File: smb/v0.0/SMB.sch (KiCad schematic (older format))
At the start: 24 parts, among them IC101 ATMEGA1284-A, J102 RTS_RESET, J103 ICSP, J104 SERIAL_REV, P101 I2C_CONN, P102 CONN_6, P103 CONN_5X2, P104 CONN_5X2, SW101 SKQGAKE010, X101 16MHz

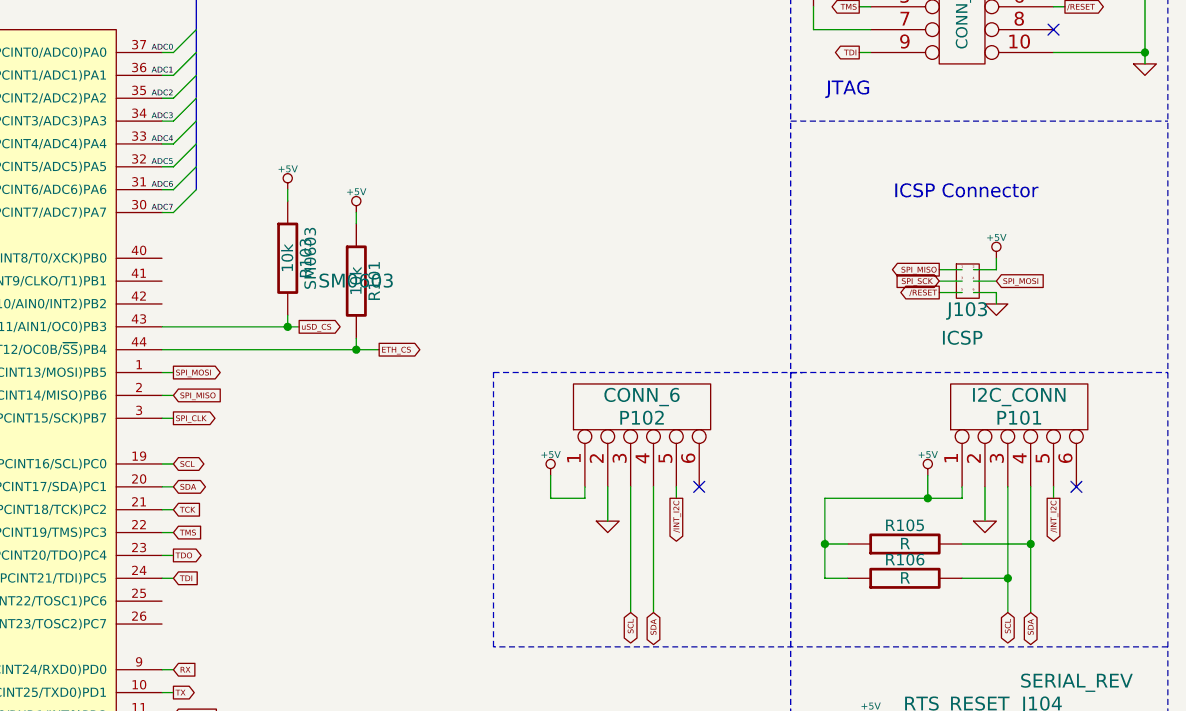
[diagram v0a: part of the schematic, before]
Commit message: Add /spare signal to the pin number 6 of the I2C connector Add silkscreen
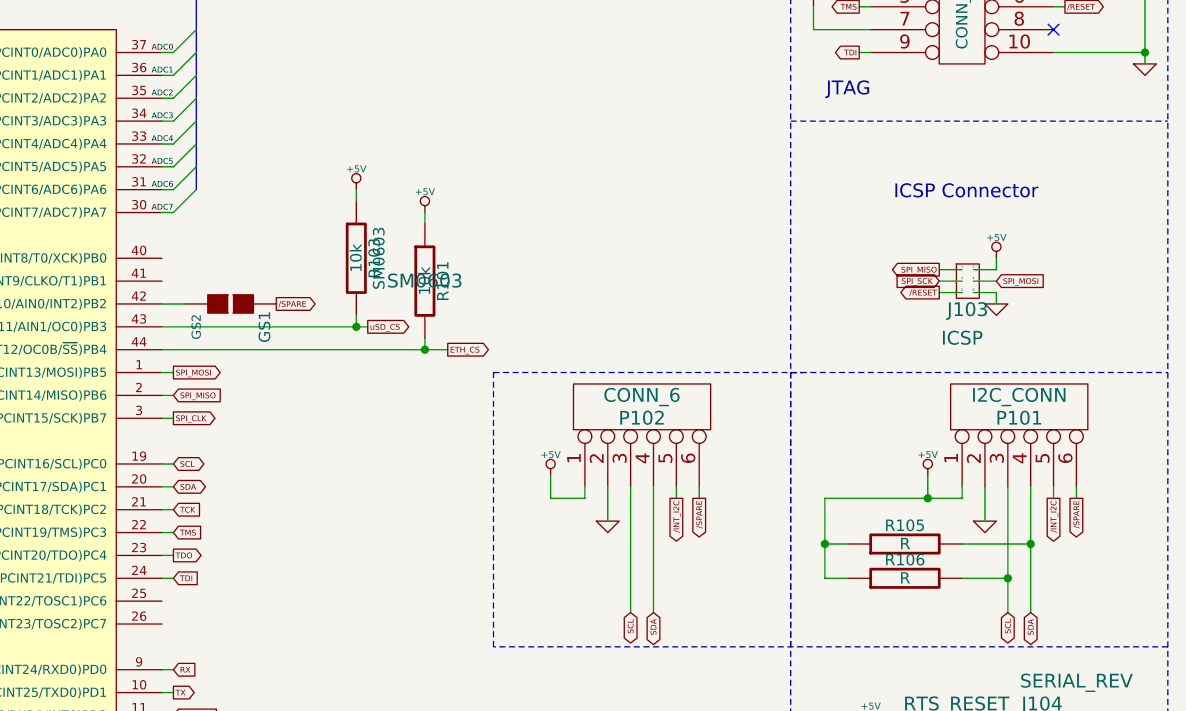
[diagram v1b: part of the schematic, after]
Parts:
- added GS1: GS2, symbol GS2
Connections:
- net at IC101.42 ((PCINT10/AIN0/INT2)PB2): now also GS1.2 (G2)
- net /SPARE: now reaches P101.6
- net /SPARE: now also P102.6, GS1.1 (G1)
- no-connect marks 3 -> 1
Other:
- moved on the sheet: R101, R103
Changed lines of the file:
@@
-EESchema Schematic File Version 2  date 09/08/2012 22:13:26
+EESchema Schematic File Version 2  date mer. 29 août 2012 13:03:19 CEST
 LIBS:power
 LIBS:device
@@
 EELAYER 25  0
 EELAYER END
-$Descr A4 11700 8267
+$Descr A4 11693 8268
 encoding utf-8
 Sheet 1 4
 Title ""
-Date "9 aug 2012"
+Date "29 aug 2012"
 Rev ""
 Comp ""
@@
 	6850 1750 6900 1750
 Wire Wire Line
-	6550 3400 7500 3400
+	6550 3400 7800 3400
 Wire Notes Line
 	10950 1400 10950 6150
@@
 	10150 4000 10150 4150
 Wire Wire Line
-	7100 2700 7100 2750
+	7400 2700 7400 2750
 Wire Notes Line
 	9300 2400 10950 2400
@@
 Wire Notes Line
 	9300 6150 10950 6150
-Connection ~ 7400 3400
-Wire Wire Line
-	7400 3350 7400 3400
+Connection ~ 7700 3400
+Wire Wire Line
+	7700 3350 7700 3400
 Wire Wire Line
 	6600 5100 6550 5100
@@
 	6600 4900 6550 4900
 Wire Wire Line
-	7400 2800 7400 2850
+	7700 2800 7700 2850
 Wire Wire Line
 	6600 4000 6550 4000
@@
 	9950 3050 10050 3050
 Wire Wire Line
-	7100 3250 7100 3300
-Connection ~ 7100 3300
+	7400 3250 7400 3300
+Connection ~ 7400 3300
 Wire Wire Line
 	9900 4050 9900 3950
@@
 	10450 1900 10500 1900
 Wire Wire Line
-	6550 3300 7150 3300
+	6550 3300 7450 3300
 Wire Wire Line
 	7700 1750 7750 1750
@@
 	1    0    0    -1
 $EndComp
-NoConn ~ 8900 4000
 $Comp
 L CONN_6 P102
@@
 	0    -1   -1   0
 $EndComp
-NoConn ~ 10550 4000
 $Comp
 L +5V #PWR08
@@
 L +5V #PWR010
 U 1 1 4FF09080
-P 7100 2700
-F 0 "#PWR010" H 7100 2790 20  0001 C CNN
-F 1 "+5V" H 7100 2790 30  0000 C CNN
-	1    7100 2700
+P 7400 2700
+F 0 "#PWR010" H 7400 2790 20  0001 C CNN
+F 1 "+5V" H 7400 2790 30  0000 C CNN
+	1    7400 2700
 	1    0    0    -1
 $EndComp
@@
 L R R103
 U 1 1 4FF09065
-P 7100 3000
-F 0 "R103" V 7180 3000 50  0000 C CNN
-F 1 "10k" V 7100 3000 50  0000 C CNN
-F 2 "SM0603" V 7200 3000 50  0000 C CNN
-	1    7100 3000
-	1    0    0    -1
-$EndComp
-Text GLabel 7150 3300 2    25   Output ~ 0
+P 7400 3000
+F 0 "R103" V 7480 3000 50  0000 C CNN
+F 1 "10k" V 7400 3000 50  0000 C CNN
+F 2 "SM0603" V 7500 3000 50  0000 C CNN
+	1    7400 3000
+	1    0    0    -1
+$EndComp
+Text GLabel 7450 3300 2    25   Output ~ 0
 uSD_CS
 $Sheet
@@
 L +5V #PWR015
 U 1 1 4FDE1AEF
-P 7400 2800
-F 0 "#PWR015" H 7400 2890 20  0001 C CNN
-F 1 "+5V" H 7400 2890 30  0000 C CNN
-	1    7400 2800
+P 7700 2800
+F 0 "#PWR015" H 7700 2890 20  0001 C CNN
+F 1 "+5V" H 7700 2890 30  0000 C CNN
+	1    7700 2800
 	1    0    0    -1
 $EndComp
@@
 L R R101
 U 1 1 4FA065D3
-P 7400 3100
-F 0 "R101" V 7480 3100 50  0000 C CNN
-F 1 "10k" V 7400 3100 50  0000 C CNN
-F 2 "SM0603" H 7400 3100 60  0000 C CNN
-	1    7400 3100
+P 7700 3100
+F 0 "R101" V 7780 3100 50  0000 C CNN
+F 1 "10k" V 7700 3100 50  0000 C CNN
+F 2 "SM0603" H 7700 3100 60  0000 C CNN
+	1    7700 3100
 	1    0    0    -1
 $EndComp
@@
 Text GLabel 6600 3500 2    25   Output ~ 0
 SPI_MOSI
-Text GLabel 7500 3400 2    25   Output ~ 0
+Text GLabel 7800 3400 2    25   Output ~ 0
 ETH_CS
 Text GLabel 6600 5100 2    25   Input ~ 0
@@
 	1    0    0    -1
 $EndComp
+$Comp
+L GS2 GS1
+U 1 1 503DF9F0
+P 6850 3200
+F 0 "GS1" H 6950 3350 50  0000 C CNN
+F 1 "GS2" H 6950 3051 40  0000 C CNN
+	1    6850 3200
+	0    1    1    0
+$EndComp
+Wire Wire Line
+	6550 3200 6650 3200
+Text GLabel 7050 3200 2    25   Output ~ 0
+/SPARE
+Text GLabel 8900 4050 3    25   Output ~ 0
+/SPARE
+Text GLabel 10550 4050 3    25   Output ~ 0
+/SPARE
+Wire Wire Line
+	8900 4000 8900 4050
+Wire Wire Line
+	10550 4000 10550 4050
 $EndSCHEMATC
